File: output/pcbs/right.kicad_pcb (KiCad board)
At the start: 2 copper layers, 141.5 x 108.2 mm, 0 parts

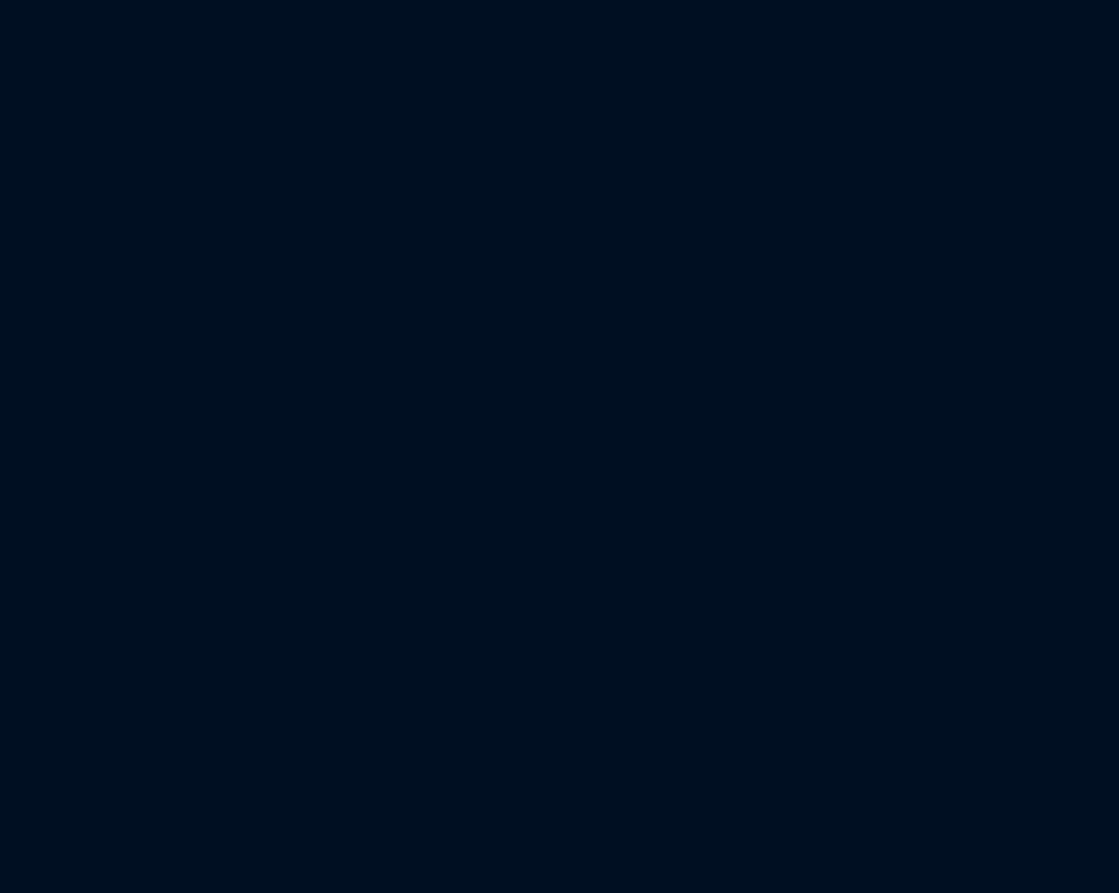
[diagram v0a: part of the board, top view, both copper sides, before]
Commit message: trying to place ts, not working. hotswap not showing up
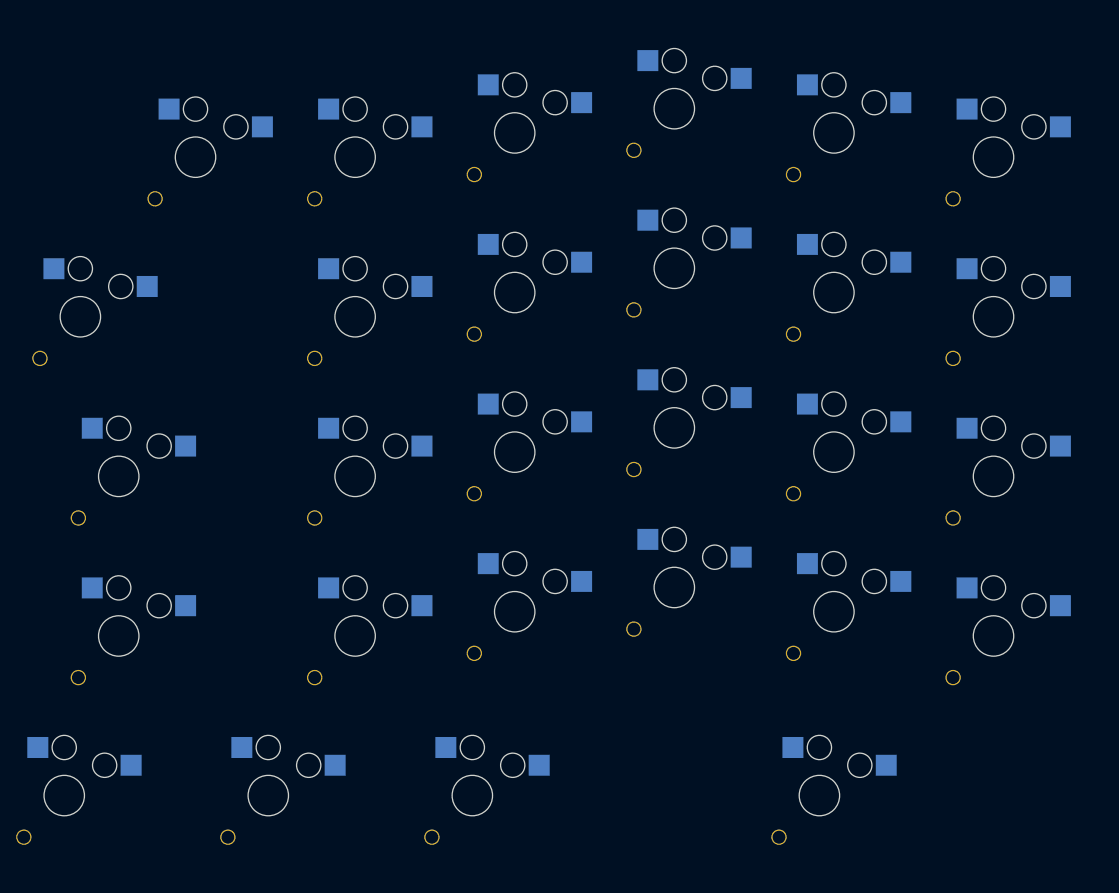
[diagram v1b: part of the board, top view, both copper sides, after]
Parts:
- added S1: , ceoloide:switch_choc_v1_v2, B.Cu at (0.00, 0.00)
- added S10: , ceoloide:switch_choc_v1_v2, B.Cu at (39.5, -25.8)
- added S11: , ceoloide:switch_choc_v1_v2, B.Cu at (39.5, -45.5)
- added S12: , ceoloide:switch_choc_v1_v2, B.Cu at (39.5, -65.2)
- added S13: , ceoloide:switch_choc_v1_v2, B.Cu at (59.2, -3.00)
- added S14: , ceoloide:switch_choc_v1_v2, B.Cu at (59.2, -22.8)
- added S15: , ceoloide:switch_choc_v1_v2, B.Cu at (59.2, -42.5)
- added S16: , ceoloide:switch_choc_v1_v2, B.Cu at (59.2, -62.2)
- added S17: , ceoloide:switch_choc_v1_v2, B.Cu at (79.0, 0.00)
- added S18: , ceoloide:switch_choc_v1_v2, B.Cu at (79.0, -19.8)
- added S19: , ceoloide:switch_choc_v1_v2, B.Cu at (79.0, -39.5)
- added S2: , ceoloide:switch_choc_v1_v2, B.Cu at (0.00, -19.8)
- added S20: , ceoloide:switch_choc_v1_v2, B.Cu at (79.0, -59.2)
- added S21: , ceoloide:switch_choc_v1_v2, B.Cu at (-29.2, 0.00)
- added S22: , ceoloide:switch_choc_v1_v2, B.Cu at (-29.2, -19.8)
- added S23: , ceoloide:switch_choc_v1_v2, B.Cu at (-34.0, -39.5)
- added S24: , ceoloide:switch_choc_v1_v2, B.Cu at (-19.8, -59.2)
- added S25: , ceoloide:switch_choc_v1_v2, B.Cu at (-36.0, 19.8)
- added S26: , ceoloide:switch_choc_v1_v2, B.Cu at (-10.7, 19.8)
- added S27: , ceoloide:switch_choc_v1_v2, B.Cu at (14.5, 19.8)
- added S28: , ceoloide:switch_choc_v1_v2, B.Cu at (57.5, 19.8)
- added S3: , ceoloide:switch_choc_v1_v2, B.Cu at (0.00, -39.5)
- added S4: , ceoloide:switch_choc_v1_v2, B.Cu at (0.00, -59.2)
- added S5: , ceoloide:switch_choc_v1_v2, B.Cu at (19.8, -3.00)
- added S6: , ceoloide:switch_choc_v1_v2, B.Cu at (19.8, -22.8)
- added S7: , ceoloide:switch_choc_v1_v2, B.Cu at (19.8, -42.5)
- added S8: , ceoloide:switch_choc_v1_v2, B.Cu at (19.8, -62.2)
- added S9: , ceoloide:switch_choc_v1_v2, B.Cu at (39.5, -6.00)
